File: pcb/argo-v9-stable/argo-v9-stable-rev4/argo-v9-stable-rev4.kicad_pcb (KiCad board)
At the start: 2 copper layers, 94.8 x 67.2 mm, 133 parts, among them IC2 MP2672GD-0000, J1 Sparkfun_NEO-N9M-SMA, J2 USB4125-GF-A, J3 LED_power_button_RGB_LED, J4 Conn_I2C_Molex_705450003, J5 Conn_I2C_Molex_705450003, K1 PRL3-5V-DC-1A, Q1 BSD840N, Q2 BSD840N, SW1 ON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

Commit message: add testpoints for CHG, CC1/2
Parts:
- added TP37: TestPoint_Probe_autonamed, Argo footprint Library:TestPoint_scope_small_autonamed, F.Cu at (132.6, 87.9)
- added TP38: TestPoint_Probe_autonamed, Argo footprint Library:TestPoint_scope_small_autonamed, F.Cu at (138.9, 87.1)
- added TP39: TestPoint_Probe_autonamed, Argo footprint Library:TestPoint_scope_small_autonamed, F.Cu at (138.3, 88.3)
- added TP40: TestPoint_Probe_autonamed, Argo footprint Library:TestPoint_scope_small_autonamed, F.Cu at (77.6, 80.5)
- IC2: value MP2672GD-0000 -> MP2672GD
- moved R35 0.31 mm to (72.2, 29.8)
- moved HB1 0.11 mm to (68.6, 29.8)
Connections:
- net Net-(J2-CC1) renamed /CC1
- net Net-(J2-CC2) renamed /CC2
- net Net-(U3-CFG) renamed /CFG
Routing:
- net /PH4: track 139.0 -> 135.9 mm, vias 10 -> 9
- net GND: track 721.2 -> 722.6 mm
- net /BAT_DIV: track 34.3 -> 35.3 mm
- net /CFG: track 3.44 -> 4.19 mm

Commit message: more testpoints and cleanup text. Add libs
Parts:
- added TP41: TestPoint_Probe_autonamed, Argo footprint Library:TestPoint_scope_small_autonamed, F.Cu at (126.4, 89.5)
- added TP42: TestPoint_Probe_autonamed, Argo footprint Library:TestPoint_scope_small_autonamed, F.Cu at (66.6, 79.9)
- IC2: value MP2672GD -> MP2672GD-0000
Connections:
- net Net-(U3-VDD) renamed /V221
- U1 pad 5: unconnected-(U1-PI7/TWI1_SCL-Pad5) -> /PI7
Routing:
- net /SW: track 30.0 -> 48.3 mm
- net /V221: track 16.7 -> 19.8 mm
- net /PI7: track 0.00 -> 2.52 mm
- net /!GPS_RESET: track 53.5 -> 51.4 mm
- net GND: vias 67 -> 68

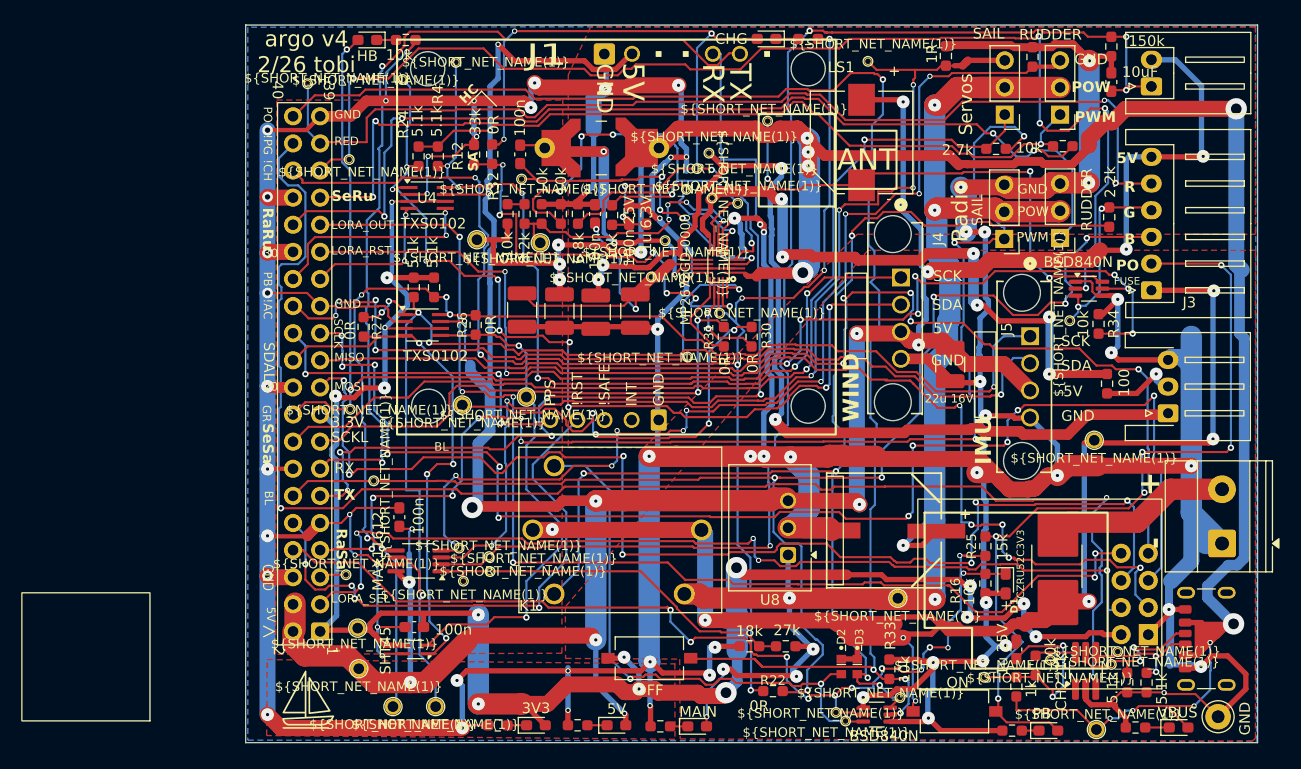
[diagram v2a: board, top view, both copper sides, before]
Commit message: jlcpcb fabricated versions of latest PCBs (rev4 argo and rev1c windsensor). For assembly on return to Zurich
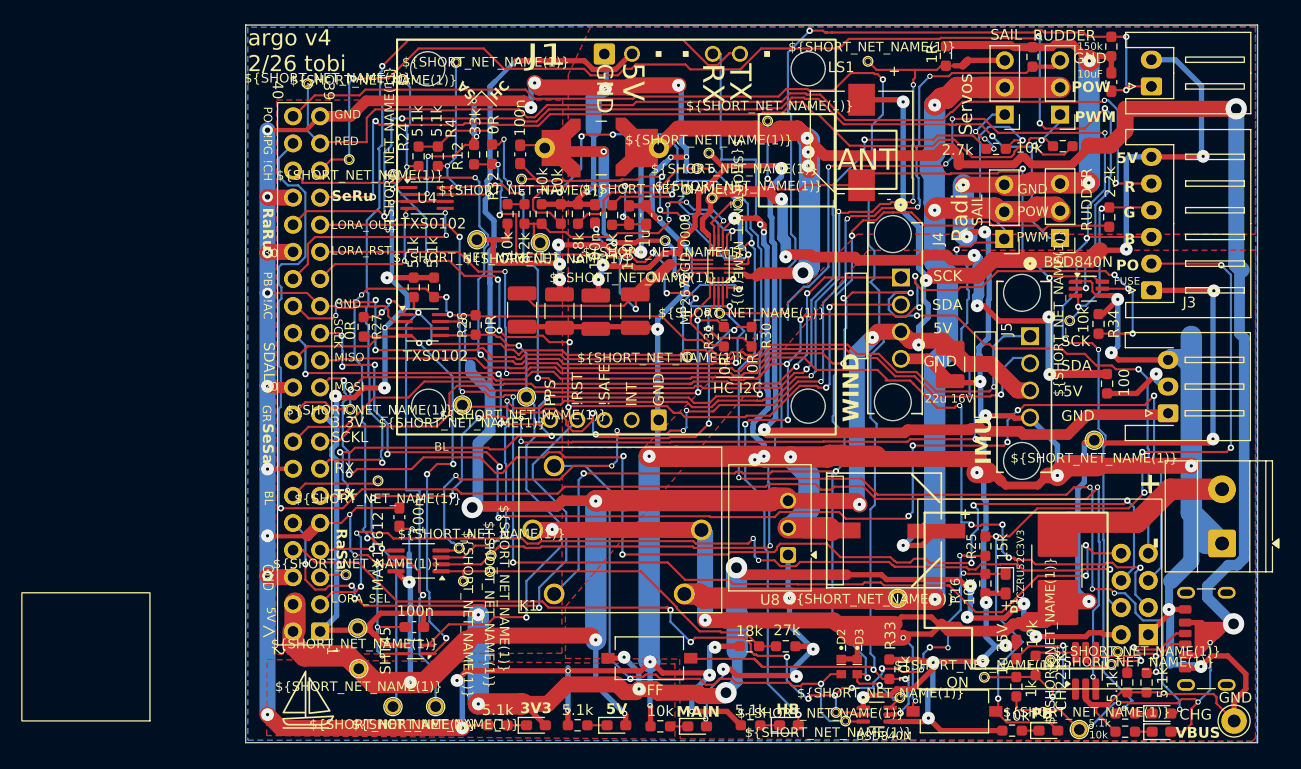
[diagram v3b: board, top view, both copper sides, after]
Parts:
- removed R22: 0R, Resistor_SMD:R_0603_1608Metric_Pad0.98x0.95mm_HandSolder
- added TP43: TestPoint_Probe_autonamed, Argo footprint Library:TestPoint_scope_small_autonamed, F.Cu at (69.6, 71.1)
- C_{BST}1: value 100n 25V -> 100n
- C_{VCC}1: value 1u 6.3V -> 1u
- R14, R20: value 5k -> 5.1k
- R19: value 1k -> 5.1k
- R35: value 10k -> 5.1k
- moved HB1 75.4 mm to (108.1, 94.0), turned to 0 degrees
- moved CHG1 73.2 mm to (143.0, 92.9), turned to 0 degrees
- moved R35 71.9 mm to (104.5, 94.0), turned to 180 degrees
- moved R19 69.8 mm to (139.6, 92.9), turned to 180 degrees
- moved TP22 28.8 mm to (71.0, 42.4)
- moved VBUS1 1.65 mm to (143.0, 94.6)
- moved TP11 1.60 mm to (135.3, 94.4)
- moved GND1 1.55 mm to (149.8, 93.6)
- moved R18 1.04 mm to (139.6, 94.6)
- moved TP31 0.22 mm to (80.2, 78.1)
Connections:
- J3 pad 3: /BLUE -> /!CHG
- TP22 pad 1: /BLUE -> /!CHG
- U1 pad 12: /BLUE -> /PI1
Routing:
- net /BLUE: track 128.4 -> 0.00 mm, vias 6 -> 0
- net /!CHG: track 135.6 -> 190.1 mm, vias 7 -> 12
- net /VCC_LDO: track 75.8 -> 128.9 mm, vias 7 -> 11
- net /PI1: track 0.00 -> 8.54 mm
- net /PH4: track 135.9 -> 143.8 mm, vias 9 -> 11
- net /VBUS: track 244.9 -> 249.8 mm
- net 5V: track 311.1 -> 307.0 mm
- net /SERVO_SAIL: track 90.6 -> 93.8 mm, vias 2 -> 5
- net /MISO: track 108.0 -> 110.8 mm
- net GND: track 722.6 -> 724.8 mm, vias 68 -> 67
- net /RADIO_RUDDER: track 98.0 -> 96.6 mm
- net /UC_RX: track 82.3 -> 81.1 mm
- net /BAT_TOP: track 93.0 -> 94.1 mm
- net /SERVO_RUDDER: track 82.9 -> 83.9 mm
- net /LORA_OUT: track 111.9 -> 112.9 mm
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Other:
- board text added: "HC I2C"

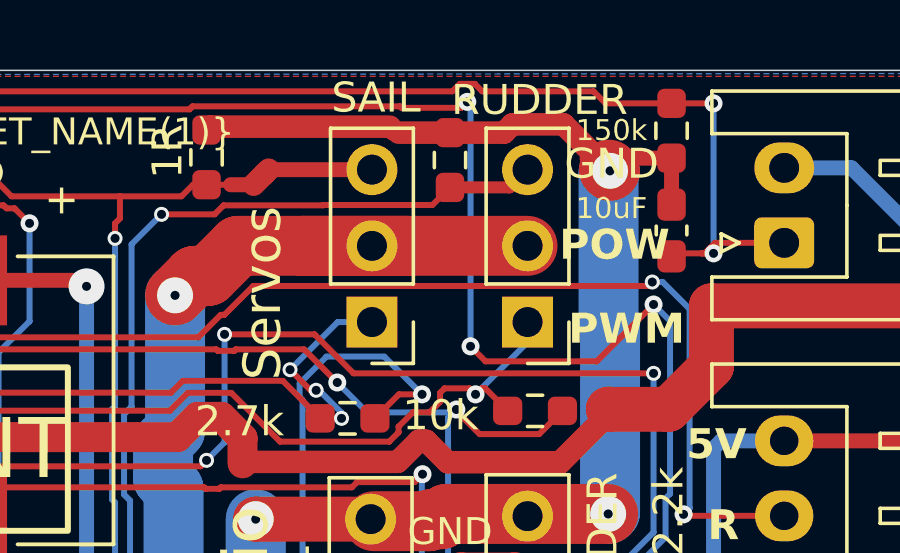
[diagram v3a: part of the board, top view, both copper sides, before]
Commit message: small edits to PCB rev 4 to note diode polarity and perhaps also missing pulldown on Buzzer
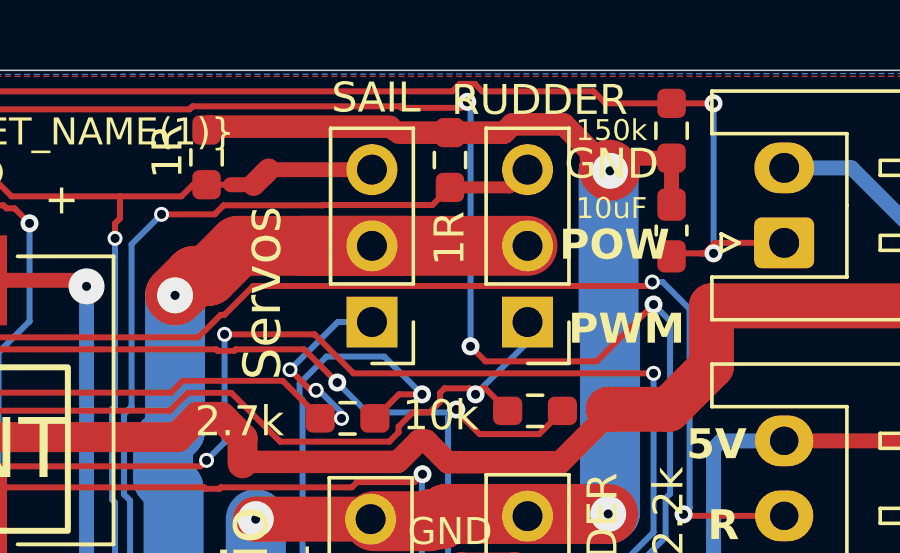
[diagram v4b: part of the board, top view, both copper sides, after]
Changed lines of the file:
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@@
 		(property "Value" "1R"
 			(at -2.610214 -0.015009 90)
-			(layer "F.Fab")
+			(layer "F.SilkS")
 			(effects
 				(font
